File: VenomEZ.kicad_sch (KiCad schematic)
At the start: 41 parts, among them CN1 HC-XH-5A-G, CN10 HC-XH-2A-G, CN2 HC-PH-8A-G, CN3 HC-XH-8A-G, CN4 HC-XH-8A-G, CN5 HC-XH-2A-G, CN6 HC-PH-7A-G, CN7 HC-XH-2A-G, CN8 HC-XH-2A-G, CN9 HC-XH-2A-G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

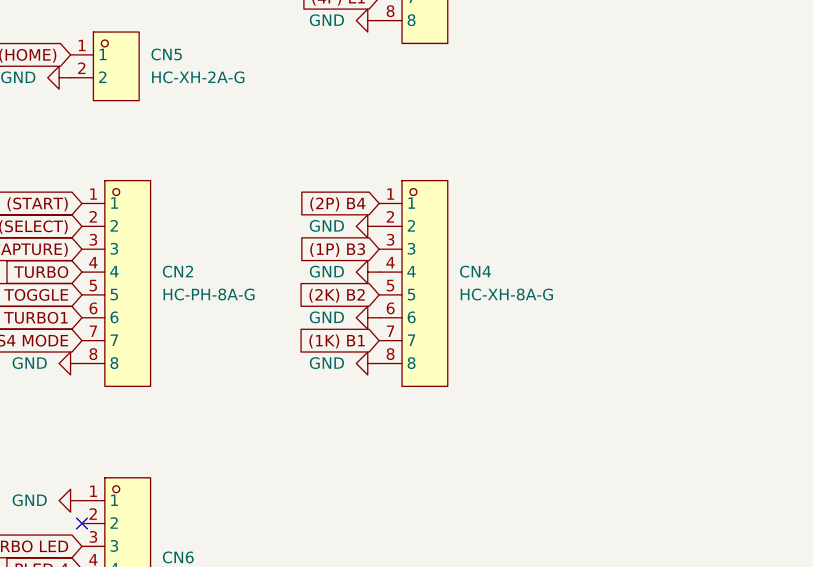
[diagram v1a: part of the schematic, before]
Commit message: Update PH connectors to ones JLC stock
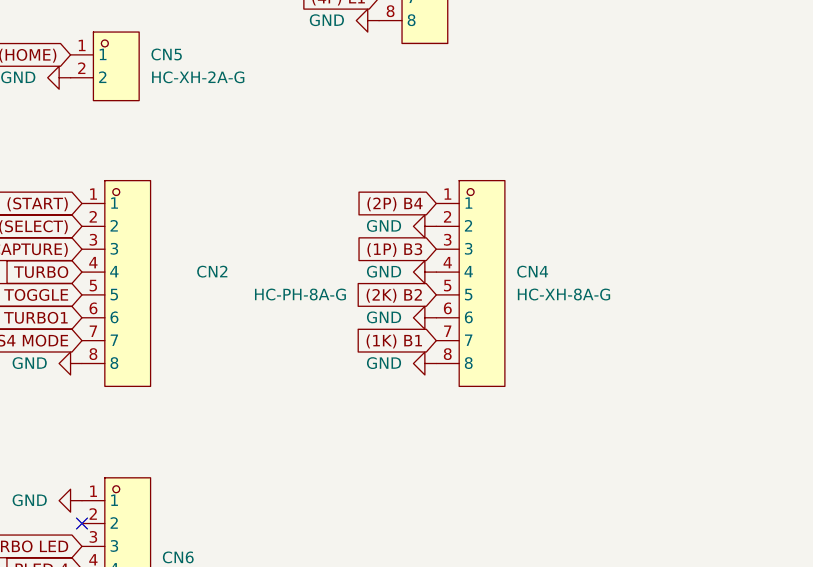
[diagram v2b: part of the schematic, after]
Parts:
- CN2: footprint easyeda2kicad:CONN-TH_8P-P2.00_HCTL_HC-PH-8A-X -> easyeda2kicad:CONN-TH_8P-P2.00_PH-8A; symbol easyeda2kicad:HC-PH-8A-G -> easyeda2kicad:PH-8A; JLC Part (none) -> Extended Part; LCSC Part C5342441 -> C33476; Manufacturer HCTL(华灿天禄) -> BOOMELE(博穆精密)
- CN6: footprint easyeda2kicad:CONN-TH_7P-P2.00_HCTL_HC-PH-7A-X -> easyeda2kicad:CONN-TH_7P-P2.00_PH-7A; symbol easyeda2kicad:HC-PH-7A-G -> easyeda2kicad:PH-7A; JLC Part (none) -> Extended Part; LCSC Part C5342440 -> C10398; Manufacturer HCTL(华灿天禄) -> BOOMELE(博穆精密)
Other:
- moved on the sheet: CN4

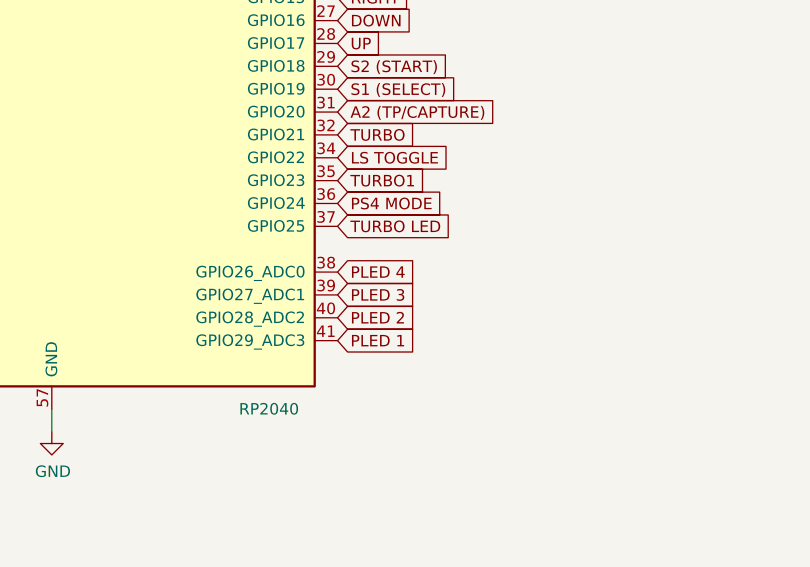
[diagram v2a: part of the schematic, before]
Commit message: Most likely fixed LED. Mounting holes enlarged.
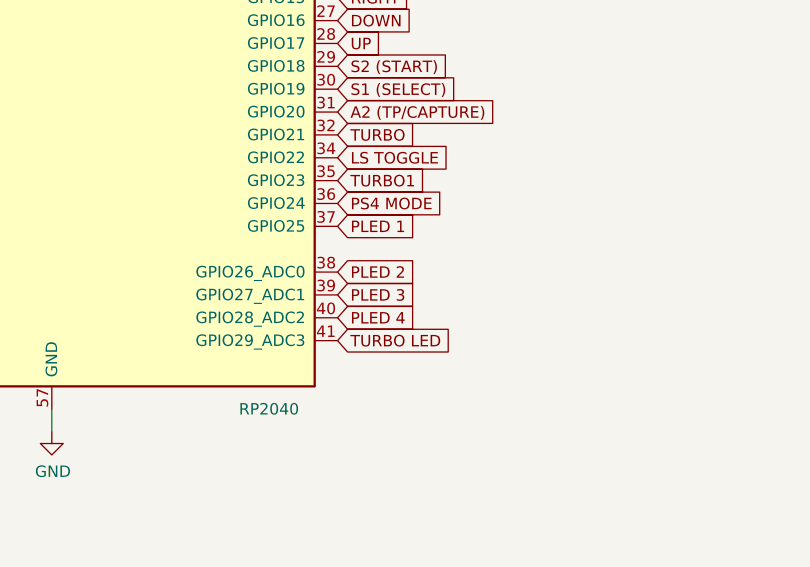
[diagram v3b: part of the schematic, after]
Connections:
- net PLED 1: now also U3.37 (GPIO25); no longer U3.41 (GPIO29_ADC3)
- net PLED 2: now also U3.38 (GPIO26_ADC0); no longer U3.40 (GPIO28_ADC2)
- net PLED 4: now also U3.40 (GPIO28_ADC2); no longer U3.38 (GPIO26_ADC0)
- net TURBO LED: now also U3.41 (GPIO29_ADC3); no longer U3.37 (GPIO25)

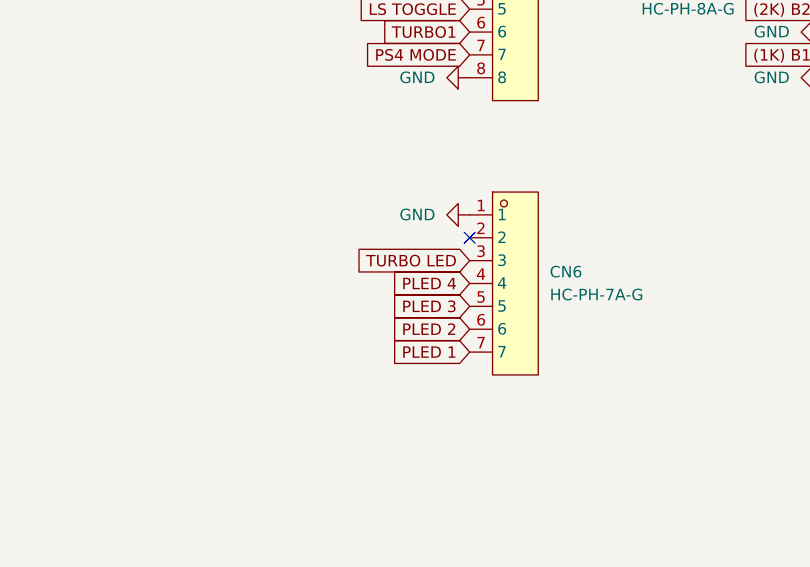
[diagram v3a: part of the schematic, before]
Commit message: Correct LED pins
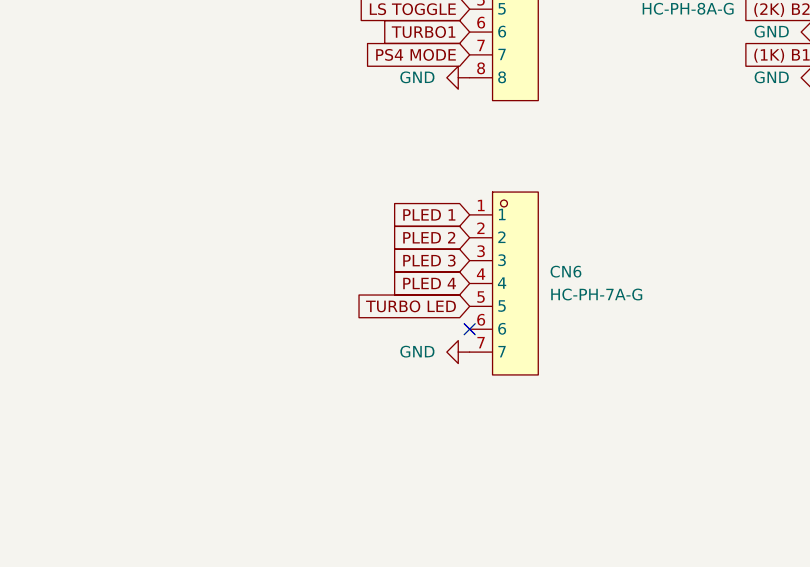
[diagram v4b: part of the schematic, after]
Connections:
- net GND: now also CN6.7; no longer CN6.1
- net PLED 1: now also CN6.1; no longer CN6.7
- net PLED 2: now also CN6.2; no longer CN6.6
- net PLED 3: now also CN6.3; no longer CN6.5
- net TURBO LED: now also CN6.5; no longer CN6.3
